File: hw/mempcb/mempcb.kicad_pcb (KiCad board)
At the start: 4 copper layers, 100 x 100 mm, 31 parts, among them J1 RC6502_Bus, J2 0.1" 2x25, U3 JEDEC_DIP32_RAM, U4 74LS138, U5 74LS138

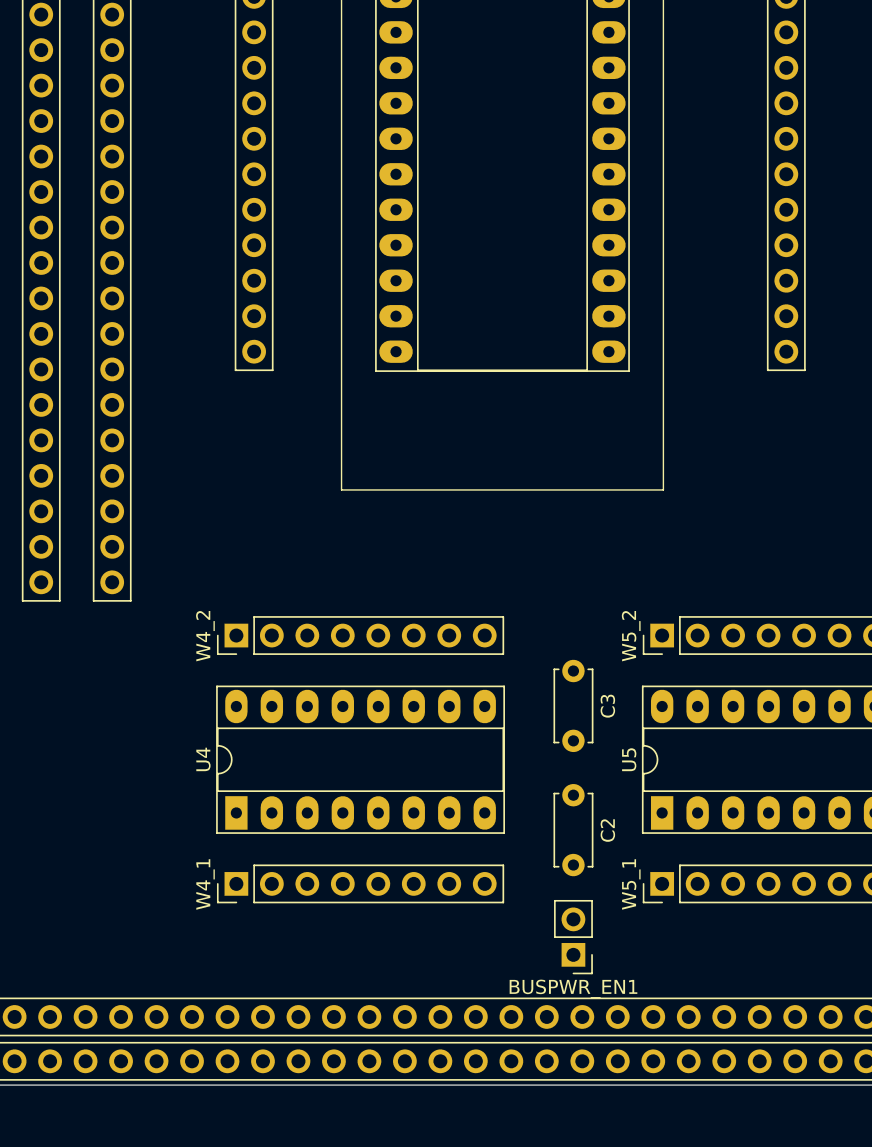
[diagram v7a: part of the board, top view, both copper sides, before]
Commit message: WIP hw/mempcb: Some preliminary routing
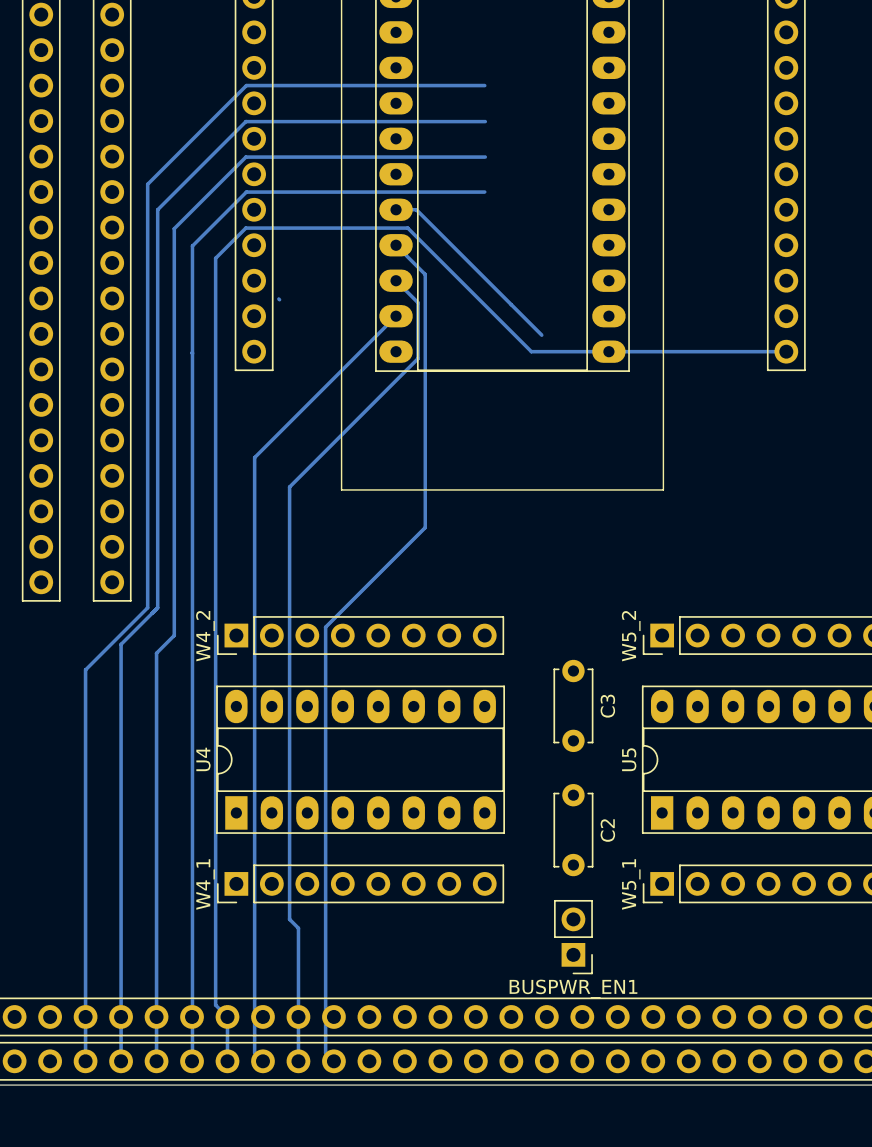
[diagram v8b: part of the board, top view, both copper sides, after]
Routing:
- net /D3: track 0.00 -> 103.3 mm
- net /D7: track 0.00 -> 91.7 mm
- net /D6: track 0.00 -> 88.6 mm
- net /D5: track 0.04 -> 84.6 mm
- net /D4: track 0.00 -> 81.0 mm
- net /D0: track 0.24 -> 62.7 mm
- net /D1: track 0.00 -> 60.6 mm
- net /D2: track 0.00 -> 57.8 mm
- net /A0: track 0.00 -> 14.2 mm
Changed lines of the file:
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@@
     (thickness 1.6002)
     (drawings 4)
-    (tracks 2)
+    (tracks 50)
     (zones 0)
     (modules 31)
@@
   (gr_line (start 180 50) (end 180 150) (layer Edge.Cuts) (width 0.0381))
   (gr_line (start 80 50) (end 180 50) (layer Edge.Cuts) (width 0.0381))
+  (segment (start 106.118118 78.448) (end 123.18 78.448) (width 0.254) (layer Back) (net 8))
+  (segment (start 99.05 85.516118) (end 106.118118 78.448) (width 0.254) (layer Back) (net 8))
+  (segment (start 99.05 115.829566) (end 99.05 85.516118) (width 0.254) (layer Back) (net 8))
+  (segment (start 94.605 120.274566) (end 99.05 115.829566) (width 0.254) (layer Back) (net 8))
+  (segment (start 94.605 148.298) (end 94.605 120.274566) (width 0.254) (layer Back) (net 8))
+  (segment (start 97.145 118.453) (end 97.145 148.298) (width 0.254) (layer Back) (net 9))
+  (segment (start 99.3675 116.2305) (end 97.145 118.453) (width 0.254) (layer Back) (net 9))
+  (segment (start 99.685 115.913) (end 99.3675 116.2305) (width 0.254) (layer Back) (net 9))
+  (segment (start 106.079119 81.026999) (end 123.218999 81.026999) (width 0.254) (layer Back) (net 9))
+  (segment (start 99.768118 87.338) (end 106.079119 81.026999) (width 0.254) (layer Back) (net 9))
+  (segment (start 99.768118 115.829882) (end 99.768118 87.338) (width 0.254) (layer Back) (net 9))
+  (segment (start 99.3675 116.2305) (end 99.768118 115.829882) (width 0.254) (layer Back) (net 9))
   (segment (start 99.635277 144.778) (end 99.594 144.778) (width 0.127) (layer Front) (net 10))
+  (segment (start 100.955 117.818) (end 100.955 88.691118) (width 0.254) (layer Back) (net 10))
+  (segment (start 106.079119 83.566999) (end 123.218999 83.566999) (width 0.254) (layer Back) (net 10))
+  (segment (start 99.685 119.088) (end 100.955 117.818) (width 0.254) (layer Back) (net 10))
+  (segment (start 100.955 88.691118) (end 106.079119 83.566999) (width 0.254) (layer Back) (net 10))
+  (segment (start 99.685 148.298) (end 99.685 119.088) (width 0.254) (layer Back) (net 10))
+  (segment (start 108.49113 93.77699) (end 108.441139 93.726999) (width 0.254) (layer Back) (net 11))
+  (segment (start 102.25694 148.26606) (end 102.225 148.298) (width 0.254) (layer Back) (net 11))
+  (segment (start 102.25694 97.613058) (end 102.25694 148.26606) (width 0.254) (layer Back) (net 11))
+  (segment (start 102.225 97.581118) (end 102.25694 97.613058) (width 0.254) (layer Back) (net 11))
+  (segment (start 106.118118 86.068) (end 123.18 86.068) (width 0.254) (layer Back) (net 11))
+  (segment (start 102.25694 89.929178) (end 106.118118 86.068) (width 0.254) (layer Back) (net 11))
+  (segment (start 102.25694 97.613058) (end 102.25694 89.929178) (width 0.254) (layer Back) (net 11))
+  (segment (start 104.765 148.298) (end 104.765 145.123) (width 0.254) (layer Back) (net 12))
+  (segment (start 126.5202 97.498) (end 144.77 97.498) (width 0.254) (layer Back) (net 12))
+  (segment (start 117.669199 88.646999) (end 126.5202 97.498) (width 0.254) (layer Back) (net 12))
+  (segment (start 106.079119 88.646999) (end 117.669199 88.646999) (width 0.254) (layer Back) (net 12))
+  (segment (start 103.915001 90.811117) (end 106.079119 88.646999) (width 0.254) (layer Back) (net 12))
+  (segment (start 103.915001 144.273001) (end 103.915001 90.811117) (width 0.254) (layer Back) (net 12))
+  (segment (start 104.765 145.123) (end 103.915001 144.273001) (width 0.254) (layer Back) (net 12))
+  (segment (start 106.708999 105.079001) (end 116.83 94.958) (width 0.254) (layer Back) (net 13))
+  (segment (start 106.708999 147.701999) (end 106.708999 105.079001) (width 0.254) (layer Back) (net 13))
+  (segment (start 107.305 148.298) (end 106.708999 147.701999) (width 0.254) (layer Back) (net 13))
+  (segment (start 109.21 107.1882) (end 109.21 138.138) (width 0.254) (layer Back) (net 14))
+  (segment (start 109.845 138.773) (end 109.845 148.298) (width 0.254) (layer Back) (net 14))
+  (segment (start 118.41101 97.98719) (end 109.21 107.1882) (width 0.254) (layer Back) (net 14))
+  (segment (start 109.21 138.138) (end 109.845 138.773) (width 0.254) (layer Back) (net 14))
+  (segment (start 118.41101 93.99901) (end 118.41101 97.98719) (width 0.254) (layer Back) (net 14))
+  (segment (start 116.83 92.418) (end 118.41101 93.99901) (width 0.254) (layer Back) (net 14))
   (segment (start 112.335277 144.778) (end 112.095 144.778) (width 0.127) (layer Front) (net 15))
+  (segment (start 118.91902 110.091978) (end 118.91902 91.96702) (width 0.254) (layer Back) (net 15))
+  (segment (start 118.91902 91.96702) (end 116.83 89.878) (width 0.254) (layer Back) (net 15))
+  (segment (start 111.788999 117.221999) (end 118.91902 110.091978) (width 0.254) (layer Back) (net 15))
+  (segment (start 111.788999 147.701999) (end 111.788999 117.221999) (width 0.254) (layer Back) (net 15))
+  (segment (start 112.385 148.298) (end 111.788999 147.701999) (width 0.254) (layer Back) (net 15))
+  (segment (start 118.284 87.338) (end 125.085 94.139) (width 0.254) (layer Back) (net 25))
+  (segment (start 116.83 87.338) (end 118.284 87.338) (width 0.254) (layer Back) (net 25))
+  (segment (start 125.085 94.139) (end 127.26299 96.31699) (width 0.254) (layer Back) (net 25))
 )
